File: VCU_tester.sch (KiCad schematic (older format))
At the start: 2 parts, among them P8 BeagleBone_Black_Header, P9 BeagleBone_Black_Header

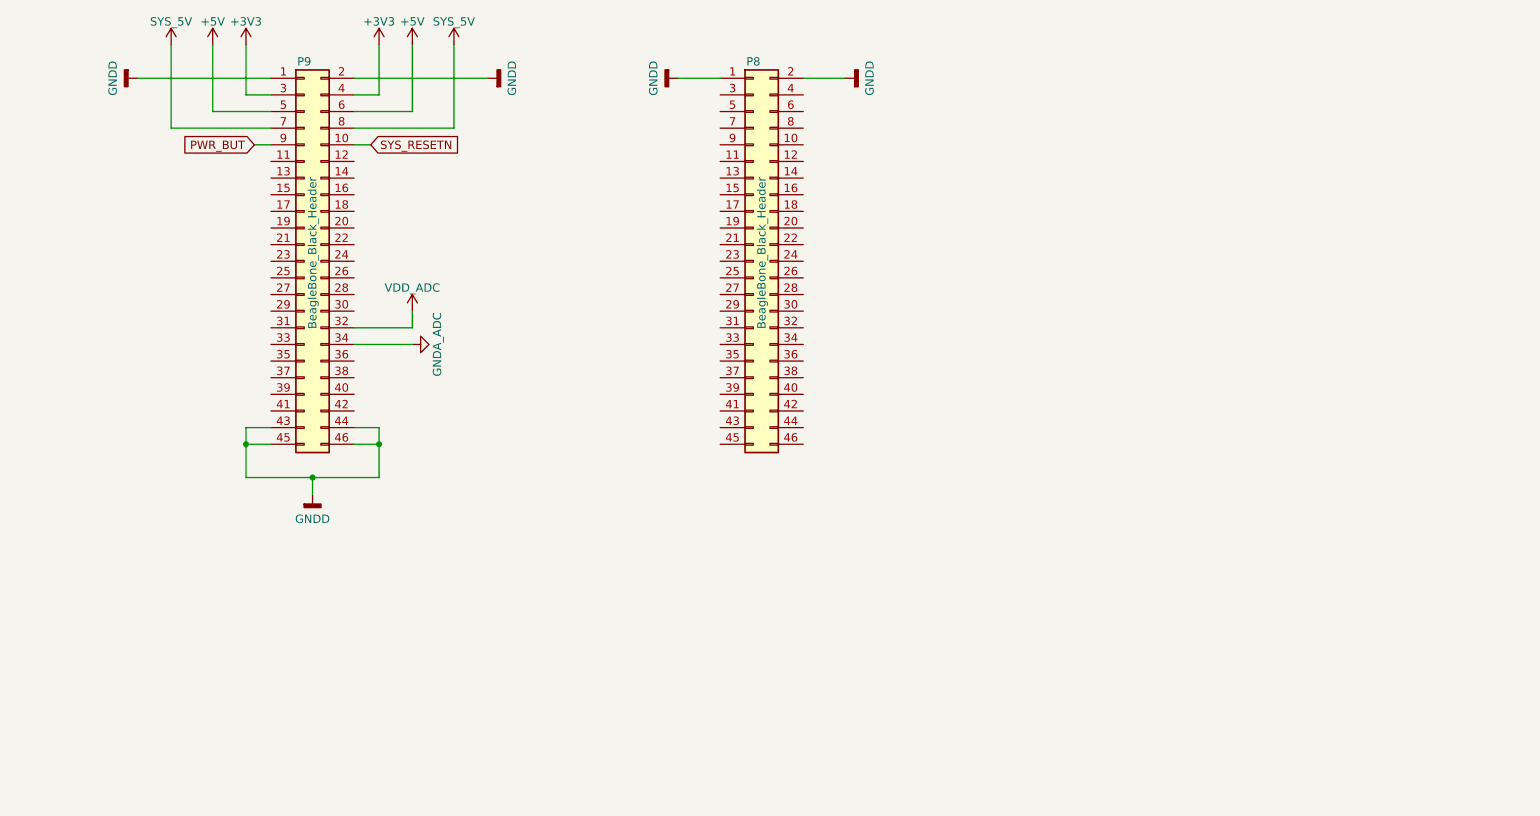
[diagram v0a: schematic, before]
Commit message: CAN parts added, rs232 parts added, gpio added
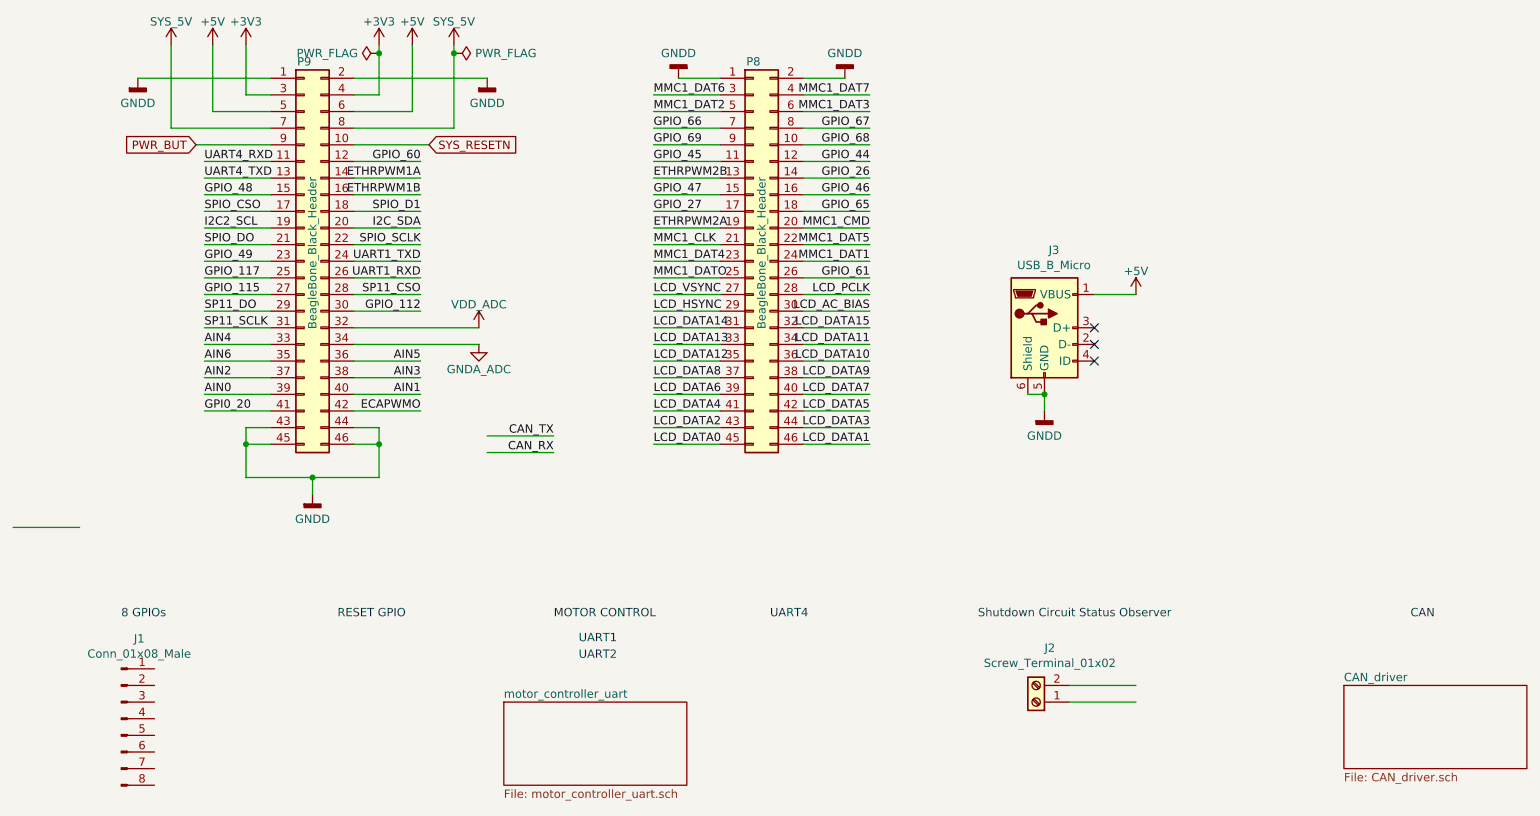
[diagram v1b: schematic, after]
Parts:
- added J1: Conn_01x08_Male, symbol Connector:Conn_01x08_Male
- added J2: Screw_Terminal_01x02, symbol Connector:Screw_Terminal_01x02
- added J3: USB_B_Micro, symbol Connector:USB_B_Micro
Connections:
- net labels added: AIN0, AIN1, AIN2, AIN3, AIN4, AIN5, AIN6, CAN_RX, CAN_TX, ECAPWMO, ETHRPWM1A, ETHRPWM1B, ETHRPWM2A, ETHRPWM2B, GPI0_20, GPIO_112, GPIO_115, GPIO_117, GPIO_26, GPIO_27, GPIO_44, GPIO_45, GPIO_46, GPIO_47, GPIO_48, GPIO_49, GPIO_60, GPIO_61, GPIO_65, GPIO_66, GPIO_67, GPIO_68, GPIO_69, I2C2_SCL, I2C_SDA, LCD_AC_BIAS, LCD_DATA0, LCD_DATA1, LCD_DATA10, LCD_DATA11, LCD_DATA12, LCD_DATA13, LCD_DATA14, LCD_DATA15, LCD_DATA2, LCD_DATA3, LCD_DATA4, LCD_DATA5, LCD_DATA6, LCD_DATA7, LCD_DATA8, LCD_DATA9, LCD_HSYNC, LCD_PCLK, LCD_VSYNC, MMC1_CLK, MMC1_CMD, MMC1_DAT1, MMC1_DAT2, MMC1_DAT3, MMC1_DAT4, MMC1_DAT5, MMC1_DAT6, MMC1_DAT7, MMC1_DATO, SP11_CSO, SP11_DO, SP11_SCLK, SPIO_CSO, SPIO_D1, SPIO_DO, SPIO_SCLK, UART1_RXD, UART1_TXD, UART4_RXD, UART4_TXD
- wire segments 32 -> 115
- no-connect marks 0 -> 3
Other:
- note added: "8 GPIOs"
- note added: "CAN"
- note added: "MOTOR CONTROL"
- note added: "RESET GPIO"
- note added: "Shutdown Circuit Status Observer"
- note added: "UART1"
- note added: "UART2"
- note added: "UART4"

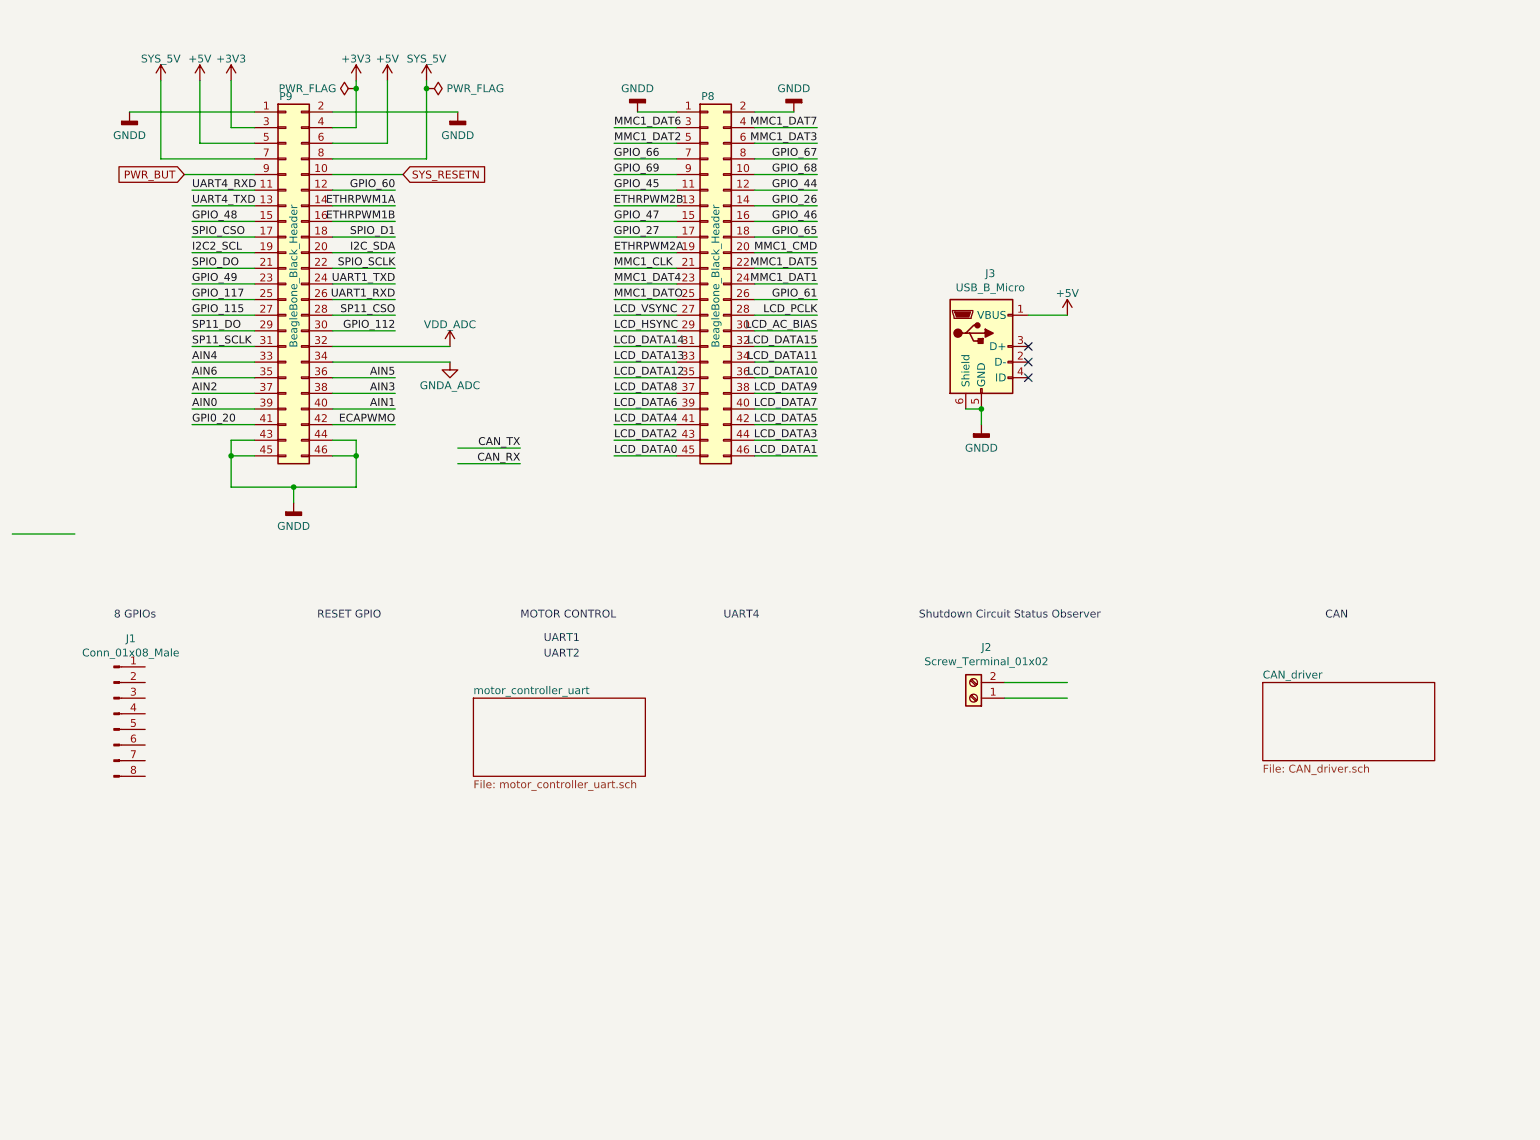
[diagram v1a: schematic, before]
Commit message: added vcu pinout, still lots needs doing
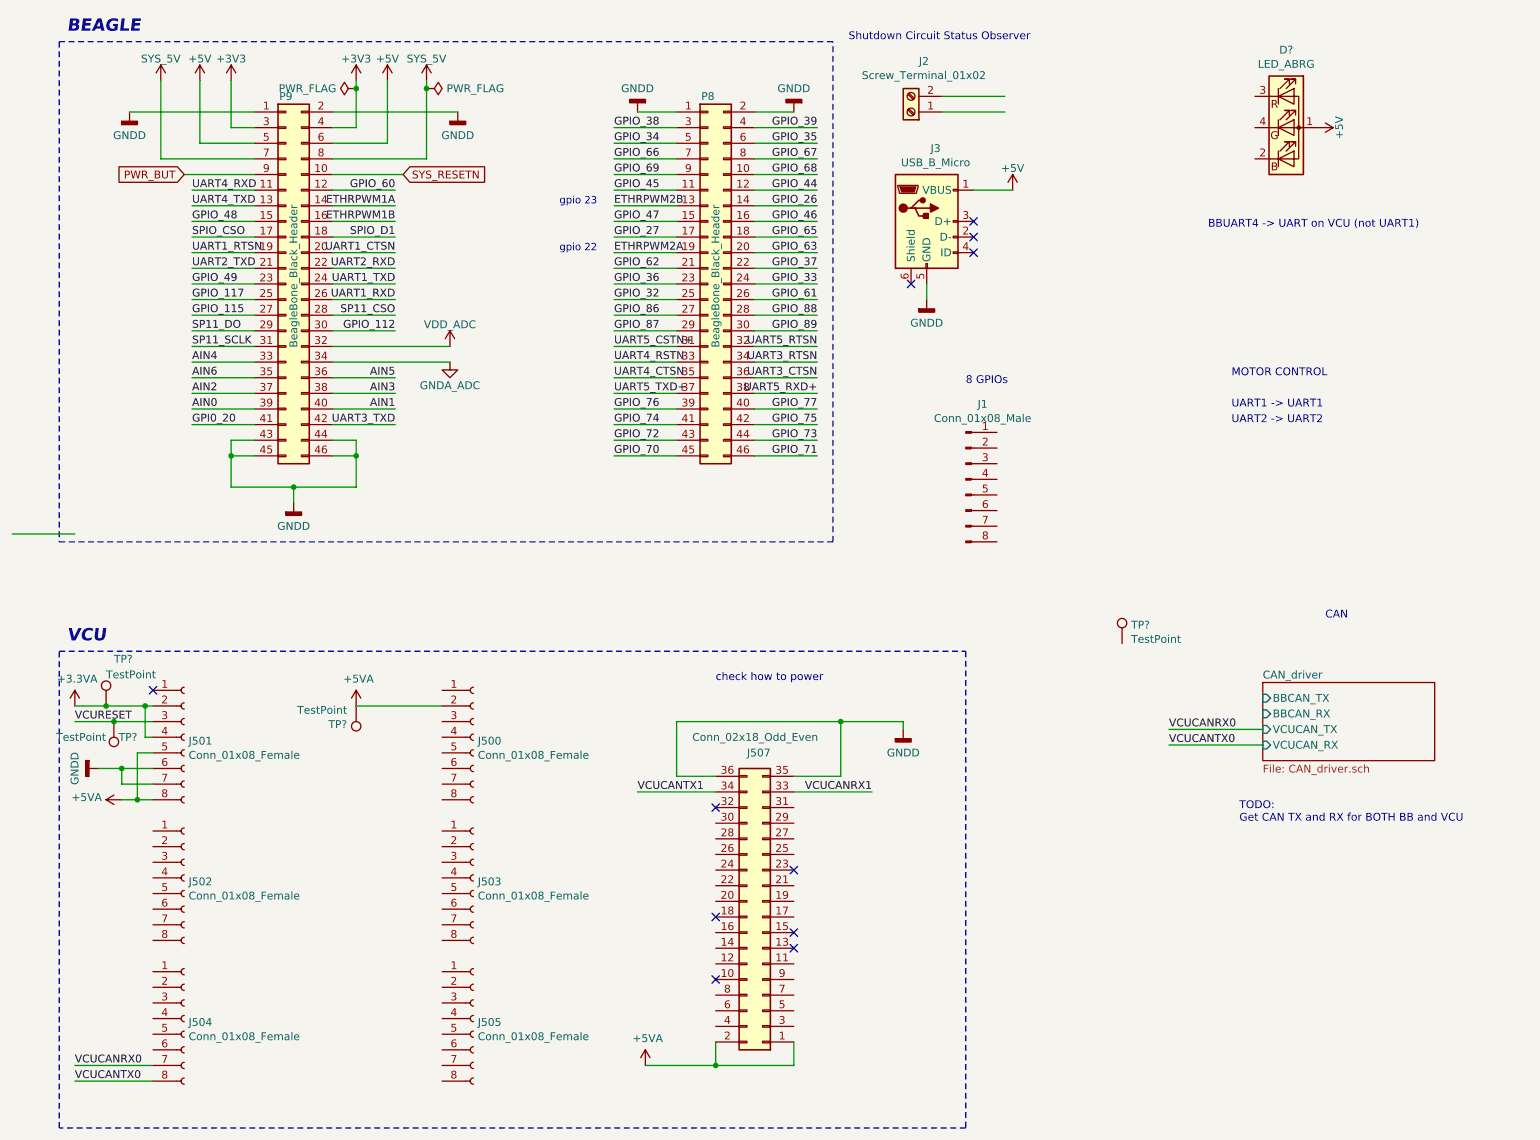
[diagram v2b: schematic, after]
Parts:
- added D?: LED_ABRG, symbol Device:LED_ABRG
- added J500, J501, J502, J503, J504, J505: Conn_01x08_Female, symbol Connector:Conn_01x08_Female
- added J507: Conn_02x18_Odd_Even, symbol Connector_Generic:Conn_02x18_Odd_Even
- added TP? (x4): TestPoint, symbol Connector:TestPoint
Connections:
- net labels added: +3.3VA, +5VA, GPIO_32, GPIO_33, GPIO_34, GPIO_35, GPIO_36, GPIO_37, GPIO_38, GPIO_39, GPIO_62, GPIO_63, GPIO_70, GPIO_71, GPIO_72, GPIO_73, GPIO_74, GPIO_75, GPIO_76, GPIO_77, GPIO_86, GPIO_87, GPIO_88, GPIO_89, UART1_CTSN, UART1_RTSN, UART2_RXD, UART2_TXD, UART3_CTSN, UART3_RTSN, UART3_TXD, UART4_CTSN, UART4_RSTN, UART5_CSTN+, UART5_RTSN, UART5_RXD+, UART5_TXD+, VCUCANRX0, VCUCANRX1, VCUCANTX0, VCUCANTX1, VCURESET
- net labels removed: CAN_RX, CAN_TX, ECAPWMO, I2C2_SCL, I2C_SDA, LCD_AC_BIAS, LCD_DATA0, LCD_DATA1, LCD_DATA10, LCD_DATA11, LCD_DATA12, LCD_DATA13, LCD_DATA14, LCD_DATA15, LCD_DATA2, LCD_DATA3, LCD_DATA4, LCD_DATA5, LCD_DATA6, LCD_DATA7, LCD_DATA8, LCD_DATA9, LCD_HSYNC, LCD_PCLK, LCD_VSYNC, MMC1_CLK, MMC1_CMD, MMC1_DAT1, MMC1_DAT2, MMC1_DAT3, MMC1_DAT4, MMC1_DAT5, MMC1_DAT6, MMC1_DAT7, MMC1_DATO, SPIO_DO, SPIO_SCLK
- wire segments 115 -> 145
- no-connect marks 3 -> 11
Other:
- note added: "BBUART4 -> UART on VCU (not UART1)"
- note added: "BEAGLE"
- note added: "TODO:\nGet CAN TX and RX for BOTH BB and VCU"
- note added: "UART1 -> UART1"
- note added: "UART2 -> UART2"
- note added: "VCU"
- note added: "check how to power"
- note added: "gpio 22"
- note added: "gpio 23"
- note removed: "RESET GPIO"
- note removed: "UART1"
- note removed: "UART2"
- note removed: "UART4"
- moved on the sheet: J1, J2, J3

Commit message: added more vcu pinout, just need to route UART, figure out GPIO problem
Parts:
- added TP?: TestPoint, symbol Connector:TestPoint
- J500: symbol Connector:Conn_01x08_Female -> Connector:Conn_01x10_Female
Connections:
- net VCURESET is gone; now on net GPIO_112: J501.3 (Pin_3), TP?.1
- net +5V: no longer D?.1 (A)
- net +5VA: no longer J500.2 (Pin_2)
- net GNDD: now also D?.1 (A), J500.7 (Pin_7), TP?.1
- net GPIO_38: now also J2.1 (Pin_1)
- net GPIO_39: now also J2.2 (Pin_2)
- net GPIO_70: now also J1.1 (Pin_1)
- net GPIO_71: now also J1.2 (Pin_2)
- net GPIO_72: now also J1.3 (Pin_3)
- net GPIO_73: now also J1.4 (Pin_4)
- net GPIO_74: now also J1.5 (Pin_5)
- net GPIO_75: now also J1.6 (Pin_6)
- net GPIO_76: now also J1.7 (Pin_7)
- net GPIO_77: now also J1.8 (Pin_8)
- net VCURXD1: now reaches J507.27 (Pin_27)
- net VCUTXD1: now reaches J507.28 (Pin_28)
- net VCURXD3: now reaches J503.1 (Pin_1)
- net VCUTXD3: now reaches J503.2 (Pin_2)
- net VCUGPIO_?: now reaches J503.4 (Pin_4)
- net VCURXD4: now reaches J505.3 (Pin_3)
- net VCUTXD4: now reaches J505.4 (Pin_4)
- net VCURXD2: now reaches J505.5 (Pin_5)
- net VCUTXD2: now reaches J505.6 (Pin_6)
- net VCURXD0: now reaches J505.7 (Pin_7)
- net VCUTXD0: now reaches J505.8 (Pin_8)
- no-connect marks 11 -> 37
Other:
- note added: "12 analog pins + 2 dac pins"
- note added: "8 GPIOs for user"
- note added: "MOTOR CONTROL\nBB VCU"
- note added: "Power / Serial iface (todo)"
- note added: "Status Indicator"
- note added: "TO ROUTE:\n8 GPIOs (only have four - I2C?), UARTMC1, UARTMC2, UART4"
- note added: "UART2 -> UART1"
- note added: "UART3 -> UART2"
- note added: "check how to power - 5V0? appears to o/p of vcu brd reg"
- note added: "need two UARTs for Motors?"
- note removed: "8 GPIOs"
- note removed: "MOTOR CONTROL"
- note removed: "UART1 -> UART1"
- note removed: "UART2 -> UART2"
- note removed: "check how to power"
- moved on the sheet: D?, J1, J3, J503, J505, P8, TP?

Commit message: vcu pinout done
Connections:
- net VCURXD2 is gone; now on net UART5_TXD+: J505.5 (Pin_5)
- net VCUTXD2 is gone; now on net UART5_RXD+: J505.6 (Pin_6)
- net GPIO_8: now reaches J500.1 (Pin_1)
- net GPIO_9: now reaches J500.2 (Pin_2)
- net GPIO_10: now reaches J500.3 (Pin_3)
- net GPIO_11: now reaches J500.4 (Pin_4)
- net GPIO_4: now reaches J503.5 (Pin_5)
- net GPIO_5: now reaches J503.6 (Pin_6)
- net GPIO_6: now reaches J503.7 (Pin_7)
- net GPIO_7: now reaches J503.8 (Pin_8)
- no-connect marks 37 -> 78
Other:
- note added: "TO ROUTE:\n8 GPIOs (only have four - I2C?), UARTMC1, UARTMC2"
- note removed: "TO ROUTE:\n8 GPIOs (only have four - I2C?), UARTMC1, UARTMC2, UART4"
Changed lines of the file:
@@
 Text Label 6150 5500 2    50   ~ 0
 VCUCANRX1
-Wire Wire Line
-	5650 5500 6150 5500
-Wire Wire Line
-	4650 5500 5150 5500
 NoConn ~ 5150 5600
 Wire Wire Line
@@
 Wire Wire Line
 	3050 5100 3600 5100
-Wire Wire Line
-	3600 6800 3000 6800
-Wire Wire Line
-	3600 6900 3000 6900
 Text Label 3000 6800 0    47   ~ 0
 VCUTXD0
@@
 VCURXD1
 Text Notes 3050 4250 0    47   ~ 0
-TO ROUTE:\n8 GPIOs (only have four - I2C?), UARTMC1, UARTMC2, UART4
+TO ROUTE:\n8 GPIOs (only have four - I2C?), UARTMC1, UARTMC2
 Wire Wire Line
 	3250 2550 3250 2300
@@
 NoConn ~ 1800 2850
 NoConn ~ 1800 2750
-Wire Wire Line
-	3600 7000 3000 7000
-Wire Wire Line
-	3600 7100 3000 7100
 Wire Wire Line
 	3600 7200 3000 7200
@@
 Text Label 3000 6300 0    47   ~ 0
 VCUGPIO_?
+Text Label 8550 3800 2    50   ~ 0
+UART2_RXD
+Text Label 8550 3900 2    50   ~ 0
+UART2_TXD
+Wire Wire Line
+	2850 6800 3600 6800
+Wire Wire Line
+	2850 6900 3600 6900
+Text Label 8550 4000 2    50   ~ 0
+UART4_RXD
+Text Label 8550 4100 2    50   ~ 0
+UART4_TXD
+Wire Wire Line
+	5650 5500 6200 5500
+Wire Wire Line
+	4550 5500 5150 5500
+Text Label 2850 7000 2    50   ~ 0
+UART5_RXD+
+Text Label 2850 7100 2    50   ~ 0
+UART5_TXD+
+Wire Wire Line
+	2850 7100 3600 7100
+Wire Wire Line
+	2850 7000 3600 7000
+Wire Wire Line
+	3600 6200 3000 6200
+Wire Wire Line
+	3600 6100 3000 6100
+Wire Wire Line
+	3600 6000 3000 6000
+Wire Wire Line
+	3600 5900 3000 5900
+Wire Wire Line
+	3600 5500 3000 5500
+Wire Wire Line
+	3600 5400 3000 5400
+Wire Wire Line
+	3600 5600 3000 5600
+Wire Wire Line
+	3600 5700 3000 5700
+Text Label 3000 6200 0    50   ~ 0
+GPIO_4
+Text Label 3000 6100 0    50   ~ 0
+GPIO_5
+Text Label 3000 6000 0    50   ~ 0
+GPIO_6
+Text Label 3000 5900 0    50   ~ 0
+GPIO_7
+Text Label 3000 5700 0    50   ~ 0
+GPIO_8
+Text Label 3000 5600 0    50   ~ 0
+GPIO_9
+Text Label 3000 5500 0    50   ~ 0
+GPIO_10
+Text Label 3000 5400 0    50   ~ 0
+GPIO_11
+NoConn ~ 3000 7300
+NoConn ~ 3000 7200
+NoConn ~ 3000 6600
+NoConn ~ 3000 6500
+NoConn ~ 3000 6300
+NoConn ~ 3600 5300
+NoConn ~ 3600 5200
+NoConn ~ 3600 5000
+NoConn ~ 3600 4900
+NoConn ~ 3600 4800
+NoConn ~ 5150 5700
+NoConn ~ 5650 5700
+NoConn ~ 5650 5600
+NoConn ~ 5650 5900
+NoConn ~ 5650 6100
+NoConn ~ 5650 6200
+NoConn ~ 5650 6300
+NoConn ~ 5650 6600
+NoConn ~ 5650 6700
+NoConn ~ 5650 6800
+NoConn ~ 5650 6900
+NoConn ~ 5650 7000
+NoConn ~ 5150 7000
+NoConn ~ 5150 6900
+NoConn ~ 5150 6800
+NoConn ~ 5150 6400
+NoConn ~ 5150 6500
+NoConn ~ 5150 6600
+NoConn ~ 5150 5900
+NoConn ~ 5150 6000
+NoConn ~ 5150 6100
+NoConn ~ 5150 6200
+Text Label 9400 3800 0    47   ~ 0
+VCUTXD0
+Text Label 9400 3900 0    47   ~ 0
+VCURXD0
+Text Label 9400 4000 0    47   ~ 0
+VCUTXD2
+Text Label 9400 4100 0    47   ~ 0
+VCURXD2
+NoConn ~ 6200 5500
+NoConn ~ 4550 5500
+NoConn ~ 3100 3150
+NoConn ~ 5400 2850
+NoConn ~ 5400 2750
+NoConn ~ 4100 2750
+NoConn ~ 4100 2650
+NoConn ~ 5400 2650
+NoConn ~ 4100 2850
 $EndSCHEMATC
